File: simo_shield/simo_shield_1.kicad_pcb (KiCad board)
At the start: 2 copper layers, 5 parts, among them J1 PORT SWD, U1 YAAJ_BluePill_Part_Like_SWD_B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, U2 elemon_board, U3 flash_externa, U4 mpu6050

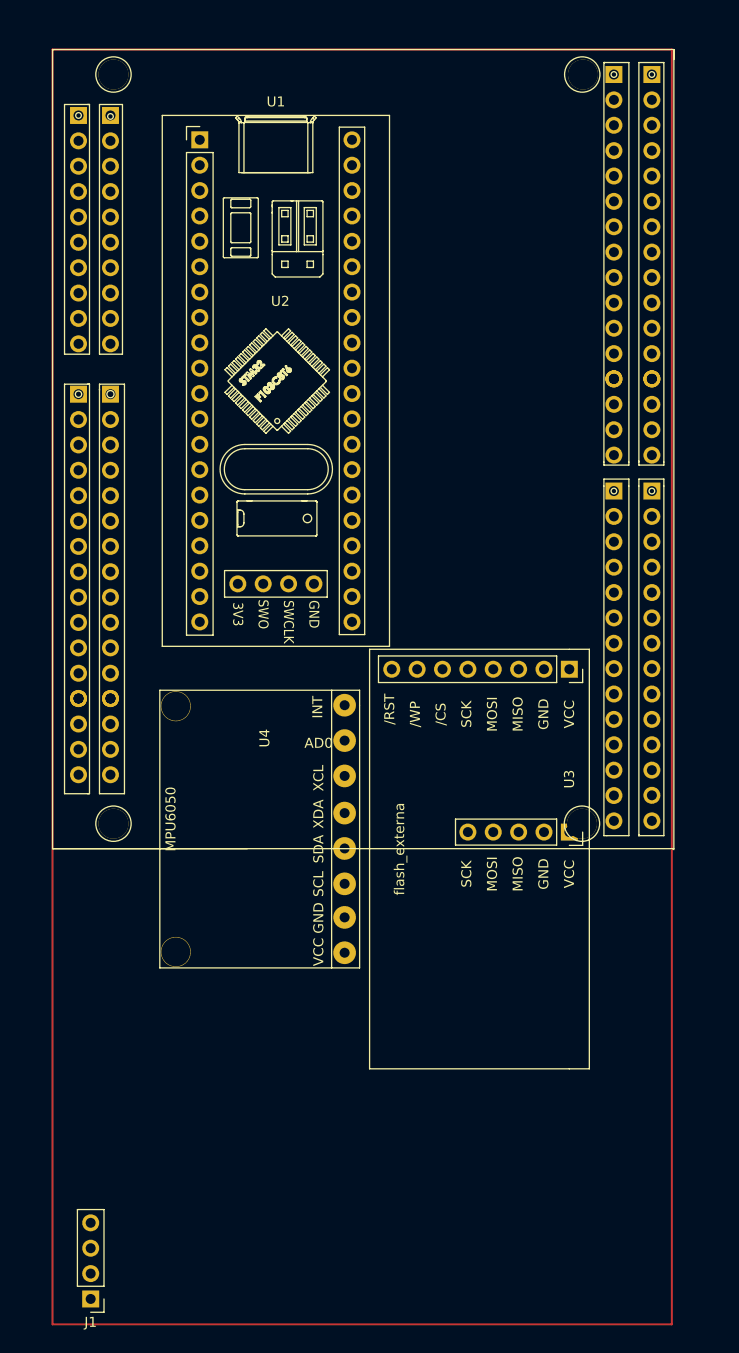
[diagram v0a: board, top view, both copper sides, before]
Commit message: organizando proyectos en carpetas: 2 proyectos    , simo_shield (principal) y simo_bateria
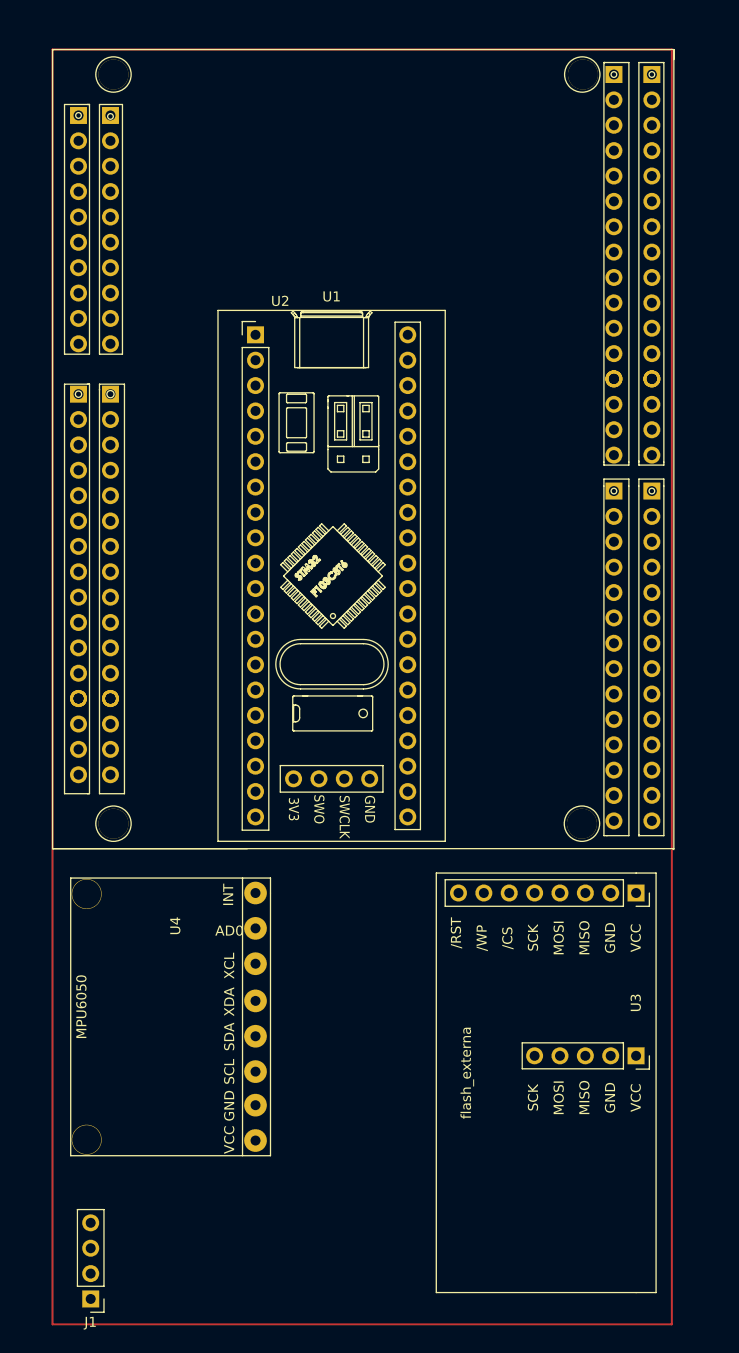
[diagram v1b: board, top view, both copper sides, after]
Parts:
- moved U3 23.4 mm to (106.7, 152.4)
- moved U4 20.8 mm to (68.6, 152.4)
- moved U1 20.3 mm to (68.6, 96.5)
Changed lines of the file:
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@@
   )
   (footprint "mpu6050:MPU6050" (layer "F.Cu")
-    (at 77.5 133.6 -90)
+    (at 68.58 152.4 -90)
     (property "Sheetfile" "simo_pcb.kicad_sch")
     (property "Sheetname" "")
@@
   )
   (footprint "simo_flash:conector_flash_ext" (layer "F.Cu")
-    (at 100 130 -90)
+    (at 106.68 152.4 -90)
     (descr "Through hole straight socket strip, 1x08, 2.54mm pitch, single row (from Kicad 4.0.7), script generated")
     (tags "Through hole socket strip THT 1x08 2.54mm single row")
@@
   )
   (footprint "simo:YAAJ_BluePill_SWD_1" (layer "F.Cu")
-    (at 63 77)
+    (at 68.58 96.52)
     (descr "Through hole headers for BluePill module. No SWD breakout. Fancy silkscreen.")
     (tags "module BlluePill Blue Pill header SWD breakout")

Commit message: se completaron todos los modelos 3d y se verifico las footprint
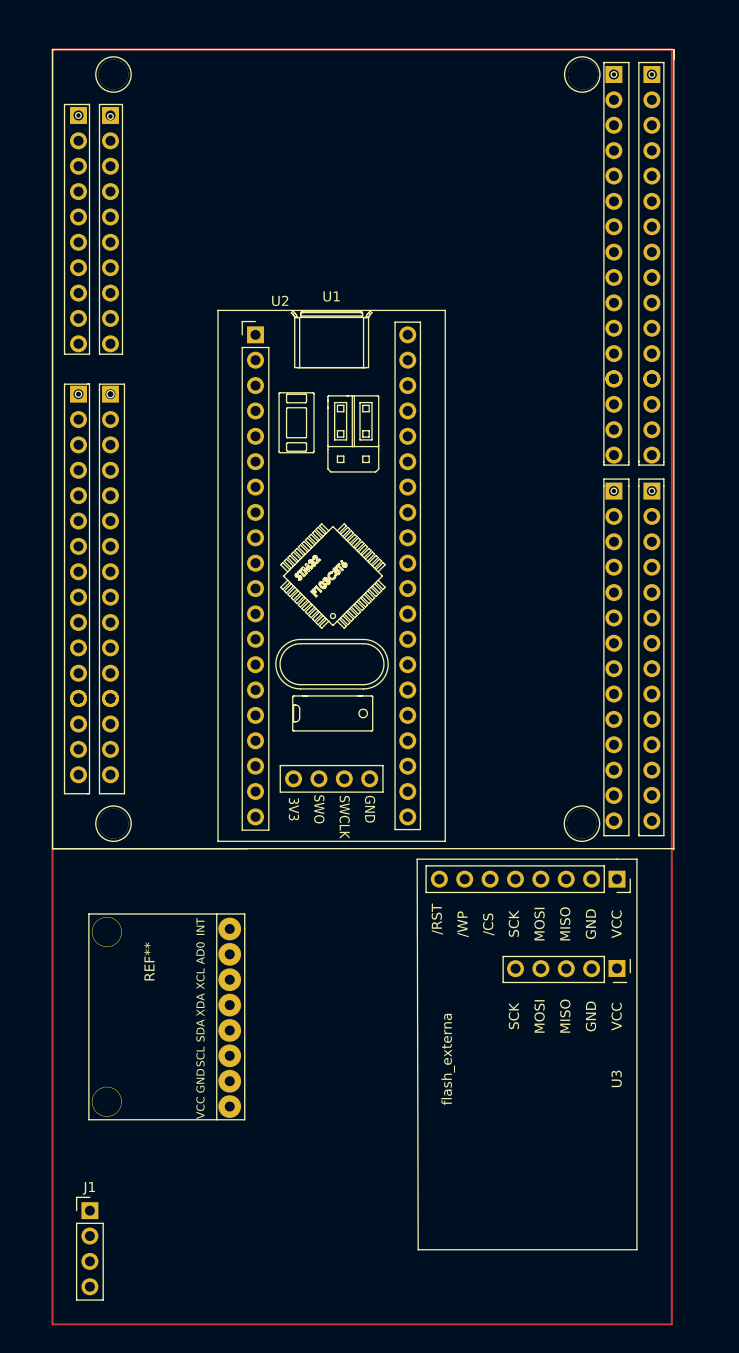
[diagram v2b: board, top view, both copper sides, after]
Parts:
- removed U4: mpu6050, mpu6050:MPU6050
- added REF**: MPU6050, simo_mpu6050:MPU6050, F.Cu at (66.0, 156.0)
- moved J1 8.84 mm to (52.0, 184.2), turned to 0 degrees
- moved U3 2.36 mm to (104.8, 151.0)
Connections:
- J1 pad 1: Net-(U1-Pad41) -> Net-(J1-Pad1)
- J1 pad 2: Net-(U1-Pad42) -> Net-(J1-Pad2)
- J1 pad 3: Net-(U1-Pad43) -> Net-(J1-Pad3)
- J1 pad 4: Net-(U1-Pad44) -> Net-(J1-Pad4)

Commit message: se hizo mas compacta pcb shield
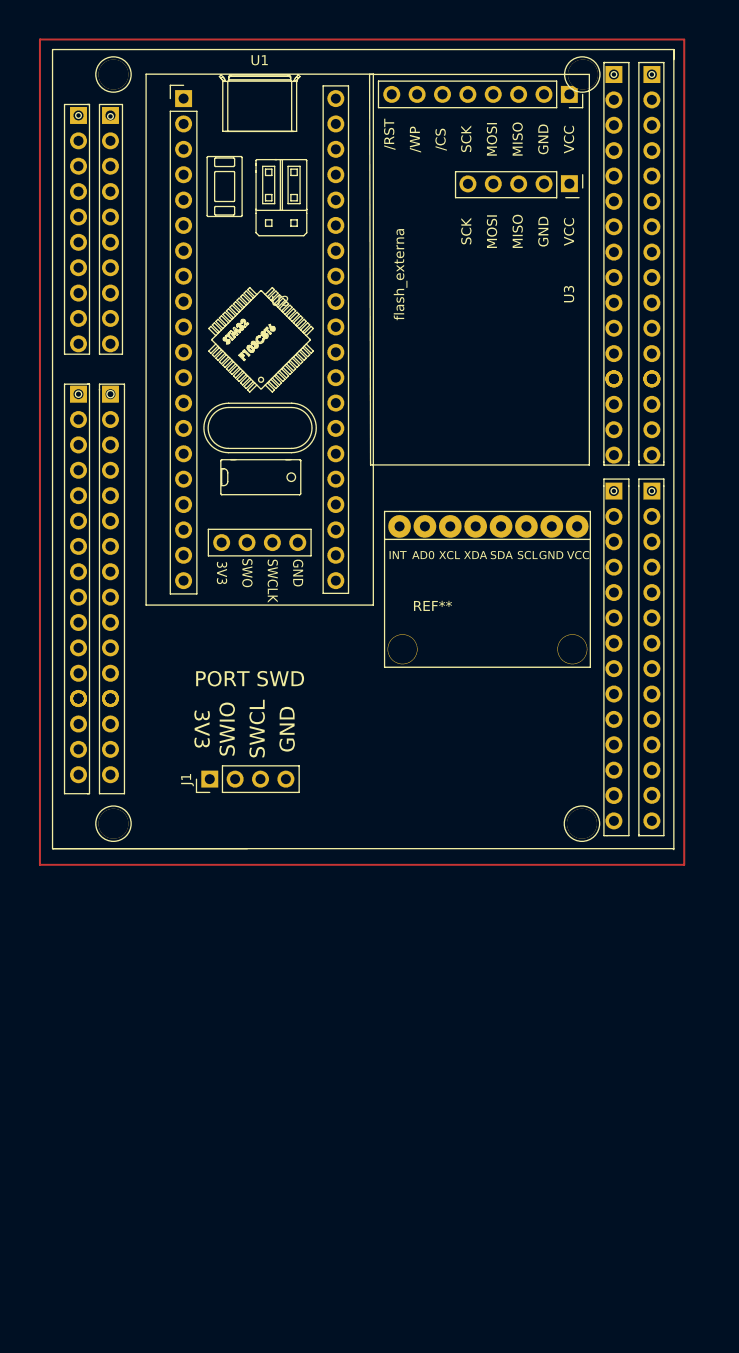
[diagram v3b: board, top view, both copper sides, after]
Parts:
- moved U3 78.7 mm to (100.0, 72.5)
- moved J1 44.8 mm to (64.0, 141.0), turned to 90 degrees
- moved REF** 43.7 mm to (83.0, 115.7), turned to 0 degrees
- moved U1 24.7 mm to (61.4, 72.9)

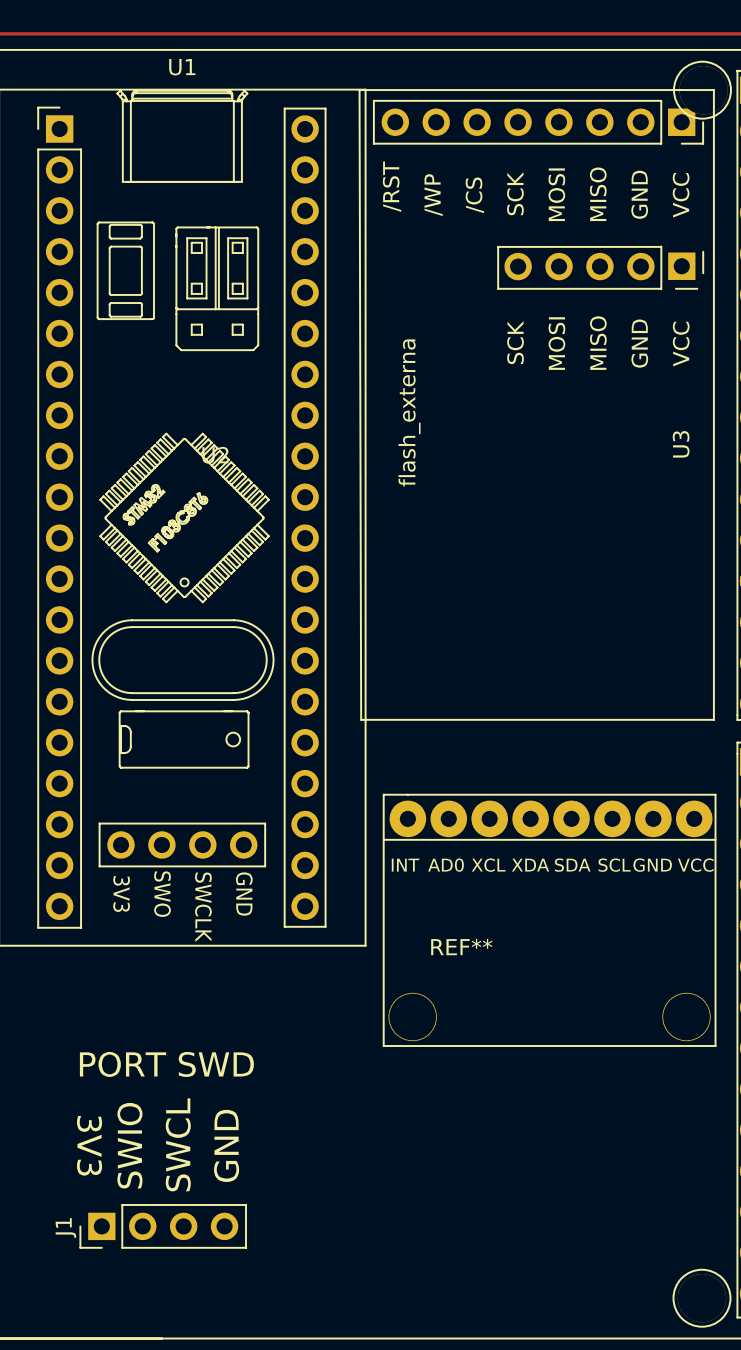
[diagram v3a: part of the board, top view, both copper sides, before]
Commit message: se agrego conector de bateria a ambas placas
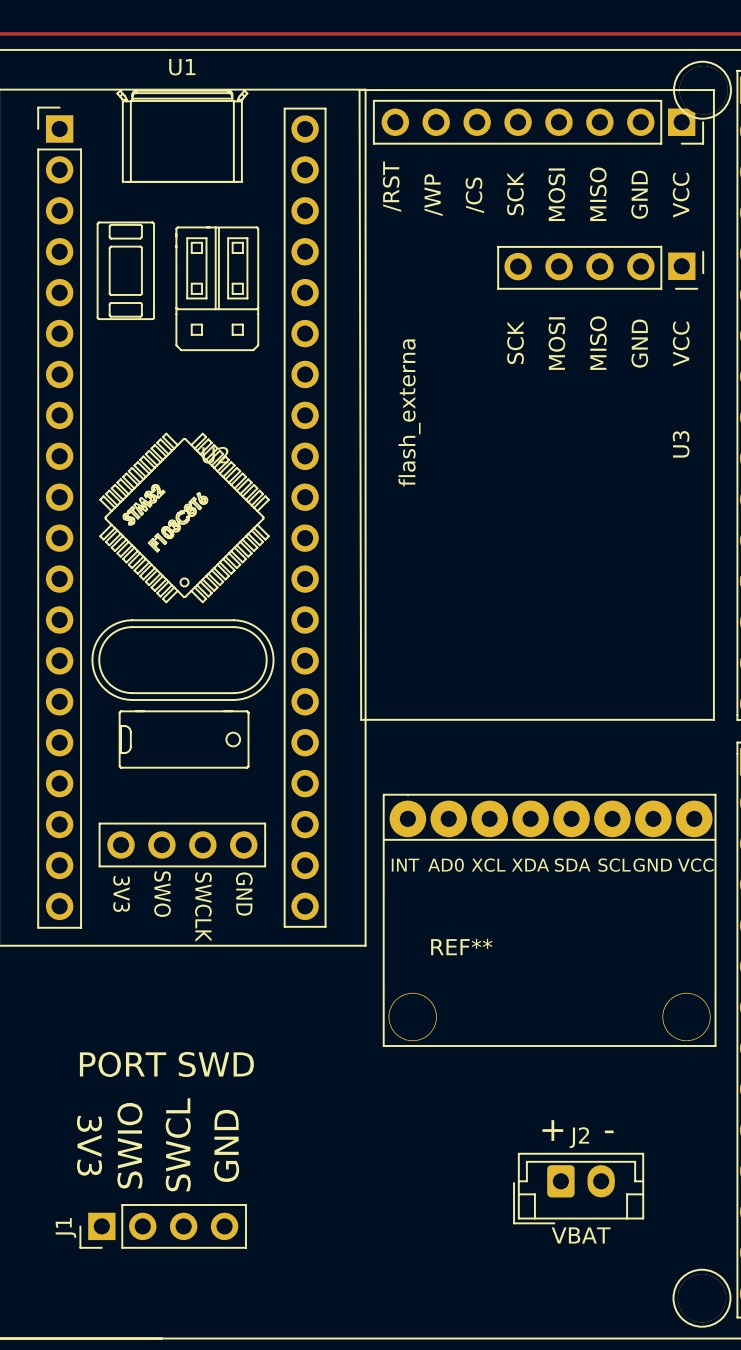
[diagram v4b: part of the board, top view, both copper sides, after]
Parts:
- added J2: VBAT, Connector_JST:JST_EH_B2B-EH-A_1x02_P2.50mm_Vertical, F.Cu at (92.5, 138.2)
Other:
- board text added: "+"
- board text added: "-"

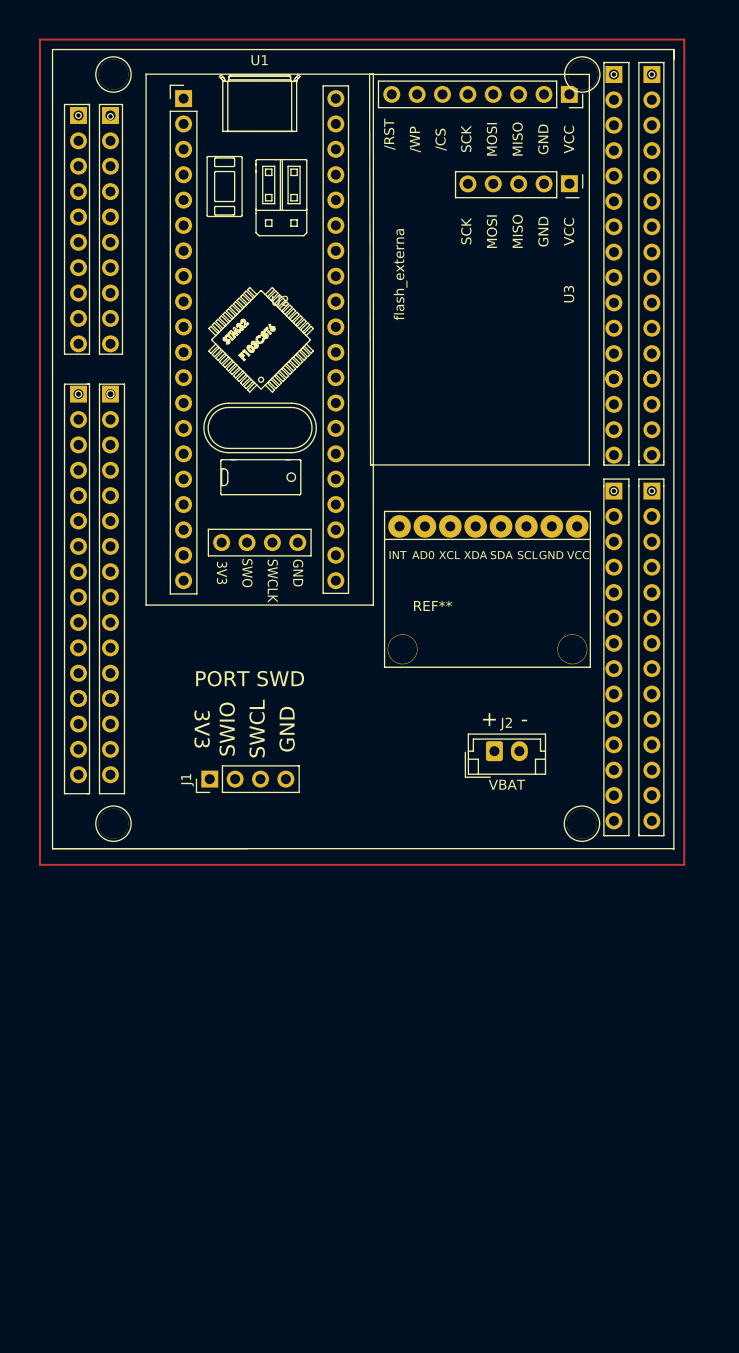
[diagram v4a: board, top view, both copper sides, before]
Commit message: se guardaron modelos 3d de ambas placas en formato step
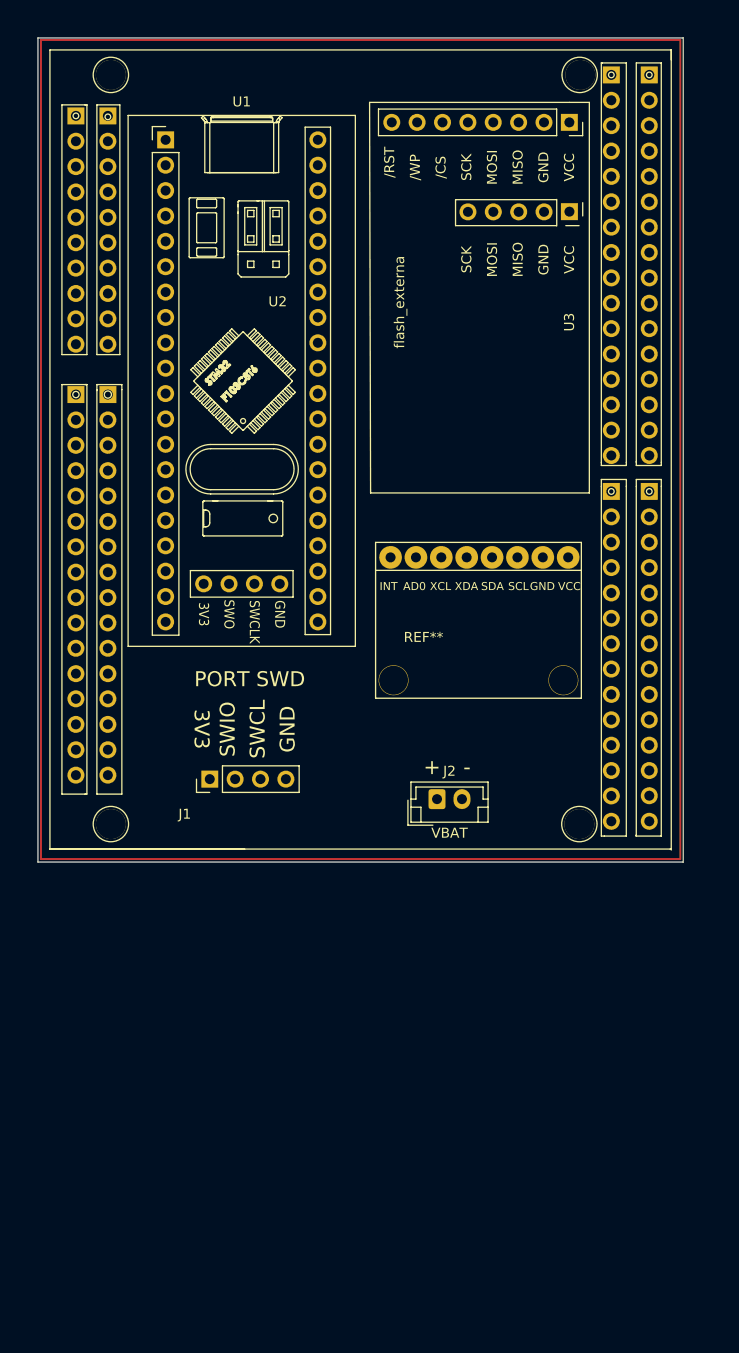
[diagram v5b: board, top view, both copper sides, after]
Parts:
- U2: footprint elemon:elemon_board -> elemon_board:elemon_board
- moved J2 7.49 mm to (86.8, 143.0)
- moved U1 4.51 mm to (59.6, 77.0)
- moved REF** 3.23 mm to (82.1, 118.8)
- moved U3 2.80 mm to (100.0, 75.2)
- moved U2 0.26 mm to (48.0, 68.0)
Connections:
- J2 pad 2: Net-(U1-Pad39) -> Net-(J2-Pad2)
- U2 pad 42: Net-(U1-Pad39) -> Net-(J2-Pad2)
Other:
- board outline added: 64.6 x 82.5 mm

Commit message: se diseñaron las pistas de placa shield simo, revisar
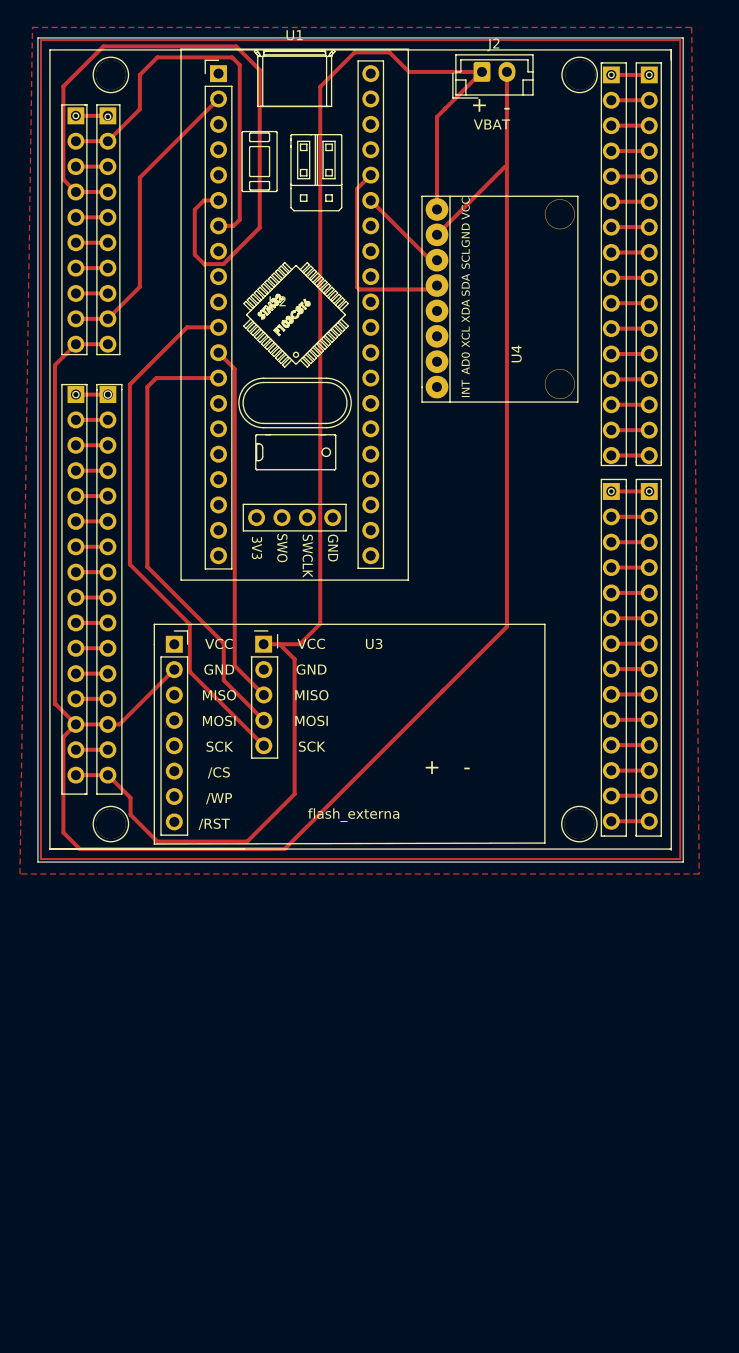
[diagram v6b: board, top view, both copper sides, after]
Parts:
- removed J1: PORT SWD, Connector_PinHeader_2.54mm:PinHeader_1x04_P2.54mm_Vertical
- removed REF**: MPU6050, simo_mpu6050:MPU6050
- added U4: mpu6050, simo_mpu6050:MPU6050, F.Cu at (86.8, 101.8)
- moved J2 72.9 mm to (91.2, 70.2)
- moved U3 65.5 mm to (60.5, 127.5), turned to 0 degrees
- moved U1 8.49 mm to (64.9, 70.4)
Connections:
- J2 pad 1: Net-(J2-Pad1) -> BAT_EXT
- J2 pad 2: Net-(J2-Pad2) -> GND_BAT
- U2 pad 10: Net-(U1-Pad19) -> GND_BAT
- U2 pad 24: Net-(U1-Pad19) -> GND_BAT
- U2 pad 26: unconnected-(U2-Pad26) -> BAT_EXT
- U2 pad 42: Net-(J2-Pad2) -> unconnected-(U2-Pad42)
- U2 pad 52: Net-(U1-Pad1) -> BAT_ENA
- U3 pad 1: Net-(U1-Pad20) -> BAT_EXT
- U3 pad 2: Net-(U1-Pad19) -> GND_BAT
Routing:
- net GND_BAT: track 0.00 -> 186.5 mm
- net BAT_EXT: track 0.00 -> 137.7 mm
- net Net-(U1-Pad6): track 0.00 -> 68.1 mm
- net Net-(U1-Pad11): track 0.00 -> 53.0 mm
- net Net-(U1-Pad13): track 0.00 -> 45.7 mm
- net Net-(U1-Pad7): track 0.00 -> 40.1 mm
- net Net-(U1-Pad12): track 0.00 -> 36.1 mm
- net Net-(U1-Pad2): track 0.00 -> 29.8 mm
- net Net-(U1-Pad36): track 0.00 -> 20.0 mm
- net Net-(U1-Pad35): track 0.00 -> 9.11 mm
- net unconnected-(U2-Pad50): track 0.00 -> 3.82 mm
- net unconnected-(U2-Pad55): track 0.00 -> 3.81 mm
- net unconnected-(U2-Pad39): track 0.00 -> 3.81 mm
- net unconnected-(U2-Pad56): track 0.00 -> 3.80 mm
- net unconnected-(U2-Pad54): track 0.00 -> 3.80 mm
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- added copper zone on F.Cu, net GND_BAT
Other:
- board text removed: "3V3"
- board text removed: "GND"
- board text removed: "SWCL"
- board text removed: "SWIO"
